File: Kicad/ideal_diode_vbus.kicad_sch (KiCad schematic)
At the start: 6 parts, among them Q4 AON7422G, U6 LM74700QDBVRQ1

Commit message: not small changes
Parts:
- Q4: footprint Package_DFN_QFN:DFN-8-1EP_3x3mm_P0.5mm_EP1.7x2.4mm -> Package_DFN_QFN:DFN-8-1EP_3x3mm_P0.65mm_EP1.5x2.25mm
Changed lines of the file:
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@@
 			)
 		)
-		(property "Footprint" "Package_DFN_QFN:DFN-8-1EP_3x3mm_P0.5mm_EP1.7x2.4mm"
+		(property "Footprint" "Package_DFN_QFN:DFN-8-1EP_3x3mm_P0.65mm_EP1.5x2.25mm"
 			(at 167.64 80.01 0)
 			(effects
@@
 					(size 1.27 1.27)
 				)
-				(hide yes)
 			)
 		)

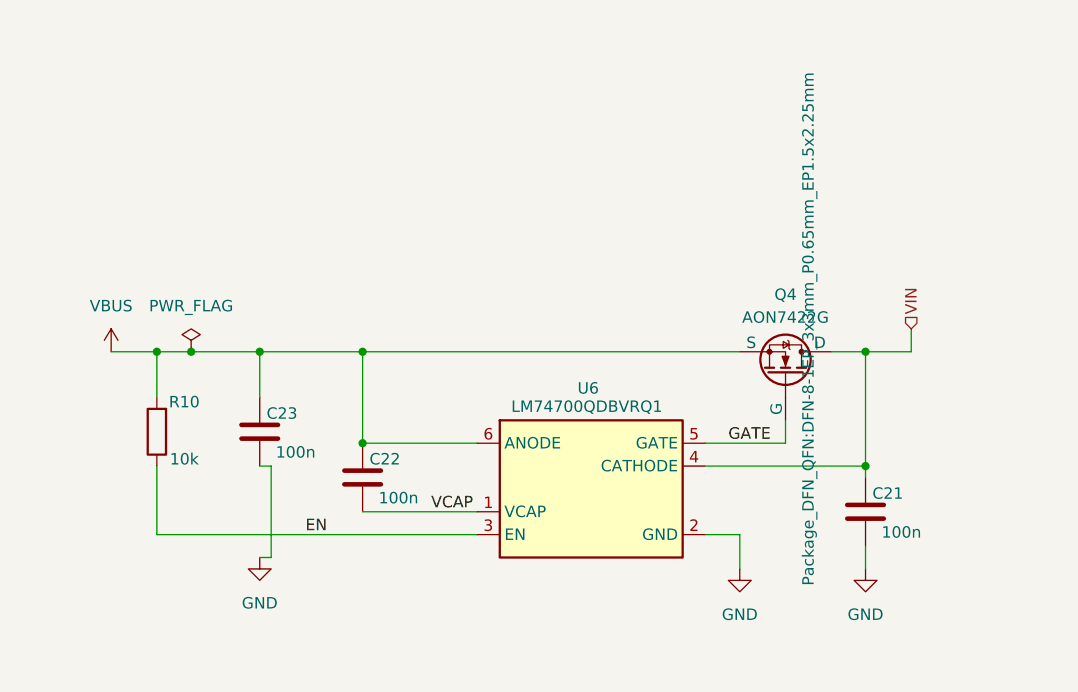
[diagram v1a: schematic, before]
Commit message: kicad schemas documentation
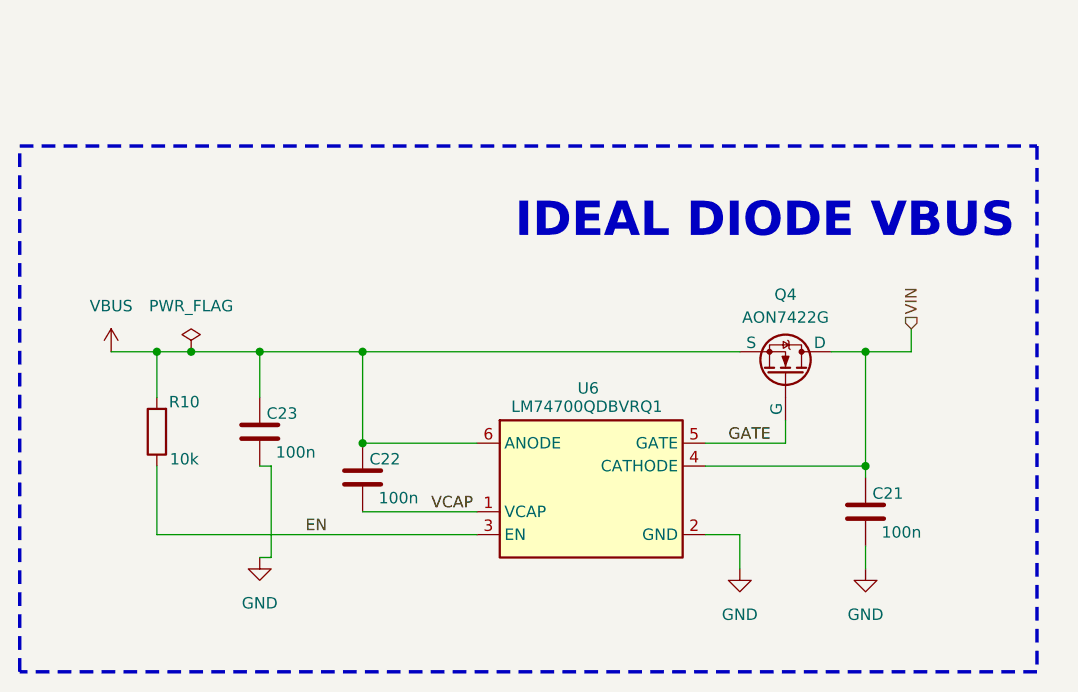
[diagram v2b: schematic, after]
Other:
- note added: "IDEAL DIODE VBUS"
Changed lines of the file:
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@@
 	(generator_version "9.0")
 	(paper "A4")
+	(rectangle
+		(start 80.01 59.69)
+		(end 193.04 118.11)
+		(stroke
+			(width 0.381)
+			(type dash)
+		)
+		(fill
+			(type none)
+		)
+	)
+	(text "IDEAL DIODE VBUS\n\n"
+		(exclude_from_sim no)
+		(at 162.814 71.12 0)
+		(effects
+			(font
+				(size 3.81 3.81)
+				(thickness 0.254)
+				(bold yes)
+			)
+		)
+	)
 	(junction
 		(at 106.68 82.55)
@@
 					(size 1.27 1.27)
 				)
-			)
-		)
+				(hide yes)
+			)
+		)
